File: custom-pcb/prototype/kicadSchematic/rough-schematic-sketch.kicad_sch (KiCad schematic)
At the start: 24 parts, among them J1 Front Panel, K1 Compressor Relay, K2 Auger Relay, M1 Compressor, M2 Auger Motor, M3 Pump, M4 Fan, Q1 Pump Mosfet, Q2 UV LED Mosfet, Q3 Fan Mosfet, SW3 Bin Switch, SW4 Float High, SW5 Float Low

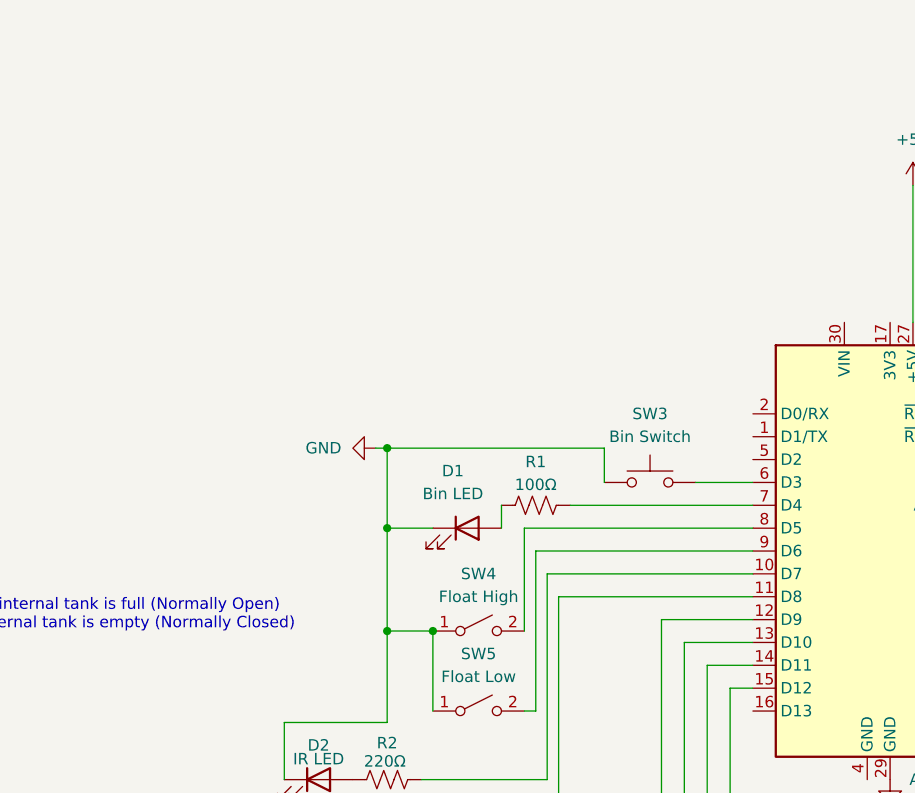
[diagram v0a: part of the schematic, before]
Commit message: add mosfet to bin LED
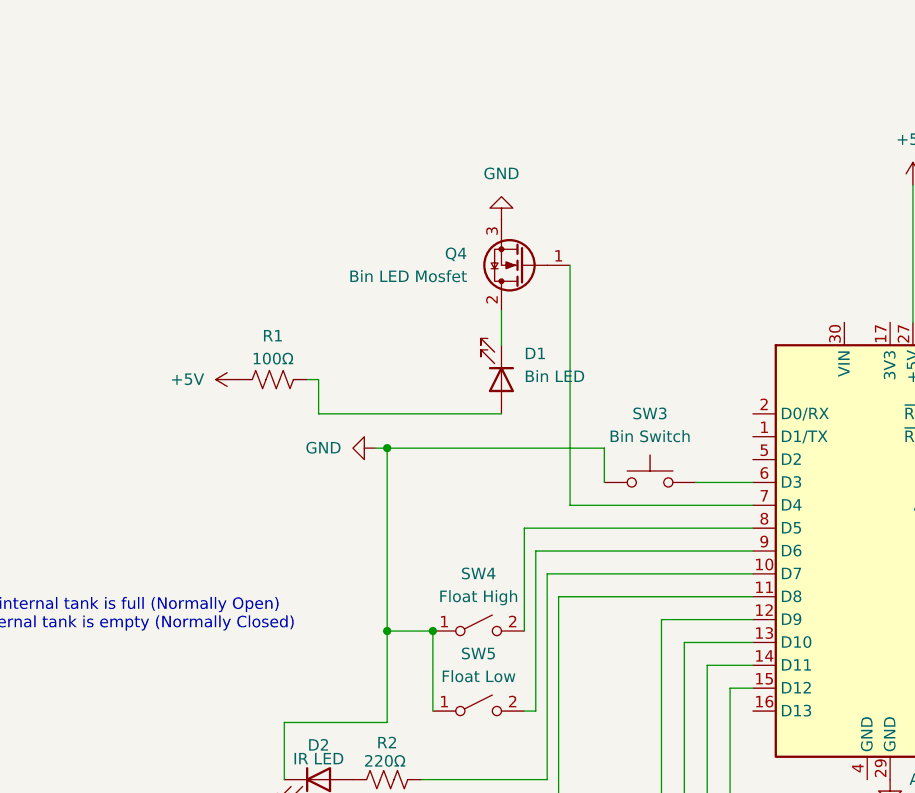
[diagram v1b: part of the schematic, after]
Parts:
- added Q4: Bin LED Mosfet, symbol Transistor_FET:Q_NMOS_GDS
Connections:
- net +5V: now also R1.1
- net GND: now also Q4.3 (S); no longer D1.1 (K)
- net at D1.2 (A): now also R1.2; no longer R1.1
- net at A1.7 (D4): now also Q4.1 (G); no longer R1.2
- new net: D1.1 (K), Q4.2 (D)
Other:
- moved on the sheet: D1, R1

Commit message: update schematic
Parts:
- added Q5: IR LED Mosfet, symbol Transistor_FET:Q_NMOS_GDS
- R1: value 100Ω -> 1kΩ
- R2: value 220Ω -> 68Ω
- R4: value 1MΩ -> 10kΩ
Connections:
- net +12V: now also R1.1
- net +5V: now also R2.1; no longer R1.1
- net GND: now also Q5.3 (S); no longer D2.1 (K)
- net at R3.1, R4.1: now also A1.16 (D13); no longer A1.20 (A1)
- net at A1.10 (D7): now also Q5.1 (G); no longer R2.2
- net at D2.2 (A): now also R2.2; no longer R2.1
- new net: D2.1 (K), Q5.2 (D)
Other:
- note removed: "When active, will hit about 1.6v"

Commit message: add a few things
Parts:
- added BZ1: Buzzer, Package_DFN_QFN:Texas_RGP0020D_VQFN-20-1EP_4x4mm_P0.5mm_EP2.7x2.7mm_ThermalVias, symbol Device:Buzzer
- R4: value 10kΩ -> 100kΩ
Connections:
- net GND: now also BZ1.2 (-)
- net at R3.1, R4.1: now also A1.5 (D2); no longer A1.16 (D13)
- new net: A1.16 (D13), BZ1.1 (+)
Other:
- note added: "I2C Bus"
- moved on the sheet: R3, R4

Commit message: switch line, not neutral
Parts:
- added C1: 10µF, symbol Device:C_Polarized
- added JP1: Debug Jumper, symbol Jumper:Jumper_2_Open
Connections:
- net GND: now also JP1.1 (A)
- net LINE: now also K1.13, K2.13; no longer M1.1, M2.1
- net NEUT: now also M1.1, MES1.2; no longer K1.13, K2.13
- net at MES1.1: now also M2.1; no longer K2.14
- net at M2.2: now also K2.14; no longer MES1.2
- net at A1.28 (~{RESET}): now also C1.1
- new net: C1.2, JP1.2 (B)

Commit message: remove buzzer, add needed components
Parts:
- removed BZ1: Buzzer, Package_DFN_QFN:Texas_RGP0020D_VQFN-20-1EP_4x4mm_P0.5mm_EP2.7x2.7mm_ThermalVias, symbol Device:Buzzer
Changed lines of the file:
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@@
-	(wire
-		(pts
-			(xy 132.08 140.97) (xy 133.35 140.97)
-		)
-		(stroke
-			(width 0)
-			(type default)
-		)
-	)
 	(wire
 		(pts
@@
 		(pts
 			(xy 83.82 78.74) (xy 104.14 78.74)
-		)
-		(stroke
-			(width 0)
-			(type default)
-		)
-	)
-	(wire
-		(pts
-			(xy 132.08 111.76) (xy 132.08 140.97)
 		)
 		(stroke
@@
 	)
 	(symbol
-		(lib_id "power:GND")
-		(at 133.35 146.05 0)
-		(unit 1)
-		(body_style 1)
-		(exclude_from_sim no)
-		(in_bom yes)
-		(on_board yes)
-		(in_pos_files yes)
-		(dnp no)
-		(fields_autoplaced yes)
-		(property "Reference" "#PWR023"
-			(at 133.35 152.4 0)
-			(hide yes)
-			(show_name no)
-			(do_not_autoplace no)
-			(effects
-				(font
-					(size 1.27 1.27)
-				)
-			)
-		)
-		(property "Value" "GND"
-			(at 133.35 151.13 0)
-			(show_name no)
-			(do_not_autoplace no)
-			(effects
-				(font
-					(size 1.27 1.27)
-				)
-			)
-		)
-		(property "Footprint" ""
-			(at 133.35 146.05 0)
-			(hide yes)
-			(show_name no)
-			(do_not_autoplace no)
-			(effects
-				(font
-					(size 1.27 1.27)
-				)
-			)
-		)
-		(property "Datasheet" ""
-			(at 133.35 146.05 0)
-			(hide yes)
-			(show_name no)
-			(do_not_autoplace no)
-			(effects
-				(font
-					(size 1.27 1.27)
-				)
-			)
-		)
-		(property "Description" "Power symbol creates a global label with name \"GND\" , ground"
-			(at 133.35 146.05 0)
-			(hide yes)
-			(show_name no)
-			(do_not_autoplace no)
-			(effects
-				(font
-					(size 1.27 1.27)
-				)
-			)
-		)
-		(pin "1"
-		)
-		(instances
-			(project "rough-schematic-sketch"
-				(path "/3caecd39-8377-4639-951b-eef5198ca2fc"
-					(reference "#PWR023")
-					(unit 1)
-				)
-			)
-		)
-	)
-	(symbol
 		(lib_id "Motor:Fan")
 		(at 219.71 116.84 270)
@@
 					(unit 1)
 				)
-			)
-		)
-	)
-	(symbol
-		(lib_id "Device:Buzzer")
-		(at 135.89 143.51 0)
-		(unit 1)
-		(body_style 1)
-		(exclude_from_sim no)
-		(in_bom yes)
-		(on_board yes)
-		(in_pos_files yes)
-		(dnp no)
-		(fields_autoplaced yes)
-		(property "Reference" "BZ1"
-			(at 139.7 142.2399 0)
-			(show_name no)
-			(do_not_autoplace no)
-			(effects
-				(font
-					(size 1.27 1.27)
-				)
-				(justify left)
-			)
-		)
-		(property "Value" "Buzzer"
-			(at 139.7 144.7799 0)
-			(show_name no)
-			(do_not_autoplace no)
-			(effects
-				(font
-					(size 1.27 1.27)
-				)
-				(justify left)
-			)
-		)
-		(property "Footprint" "Package_DFN_QFN:Texas_RGP0020D_VQFN-20-1EP_4x4mm_P0.5mm_EP2.7x2.7mm_ThermalVias"
-			(at 135.255 140.97 90)
-			(hide yes)
-			(show_name no)
-			(do_not_autoplace no)
-			(effects
-				(font
-					(size 1.27 1.27)
-				)
-			)
-		)
-		(property "Datasheet" ""
-			(at 135.255 140.97 90)
-			(hide yes)
-			(show_name no)
-			(do_not_autoplace no)
-			(effects
-				(font
-					(size 1.27 1.27)
-				)
-			)
-		)
-		(property "Description" "Buzzer, polarized"
-			(at 135.89 143.51 0)
-			(hide yes)
-			(show_name no)
-			(do_not_autoplace no)
-			(effects
-				(font
-					(size 1.27 1.27)
-				)
-			)
-		)
-		(pin "2"
-		)
-		(pin "1"
-		)
-		(instances
-			(project "rough-schematic-sketch"
-				(path "/3caecd39-8377-4639-951b-eef5198ca2fc"
-					(reference "BZ1")
-					(unit 1)
-				)
